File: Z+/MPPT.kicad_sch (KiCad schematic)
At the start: 15 parts, among them U8 LTC3130

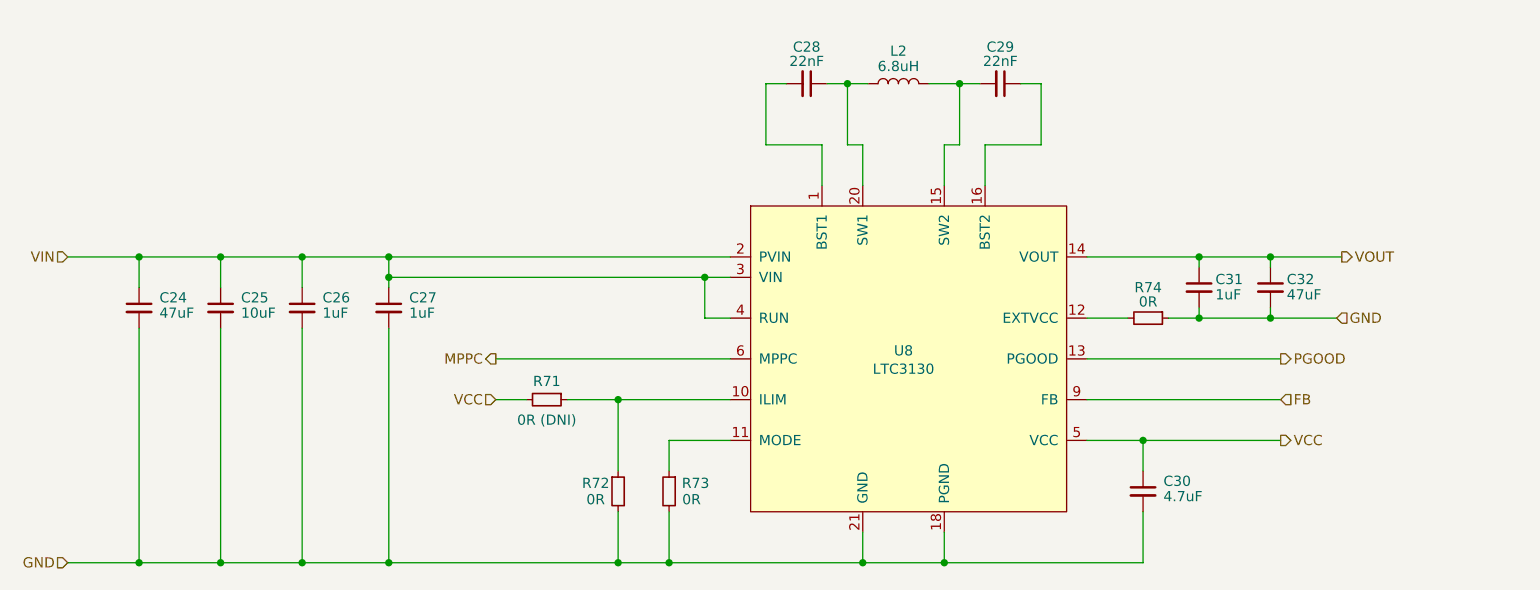
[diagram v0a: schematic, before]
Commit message: Added DRV8235, Quad Light Sensor, and refactored schematics
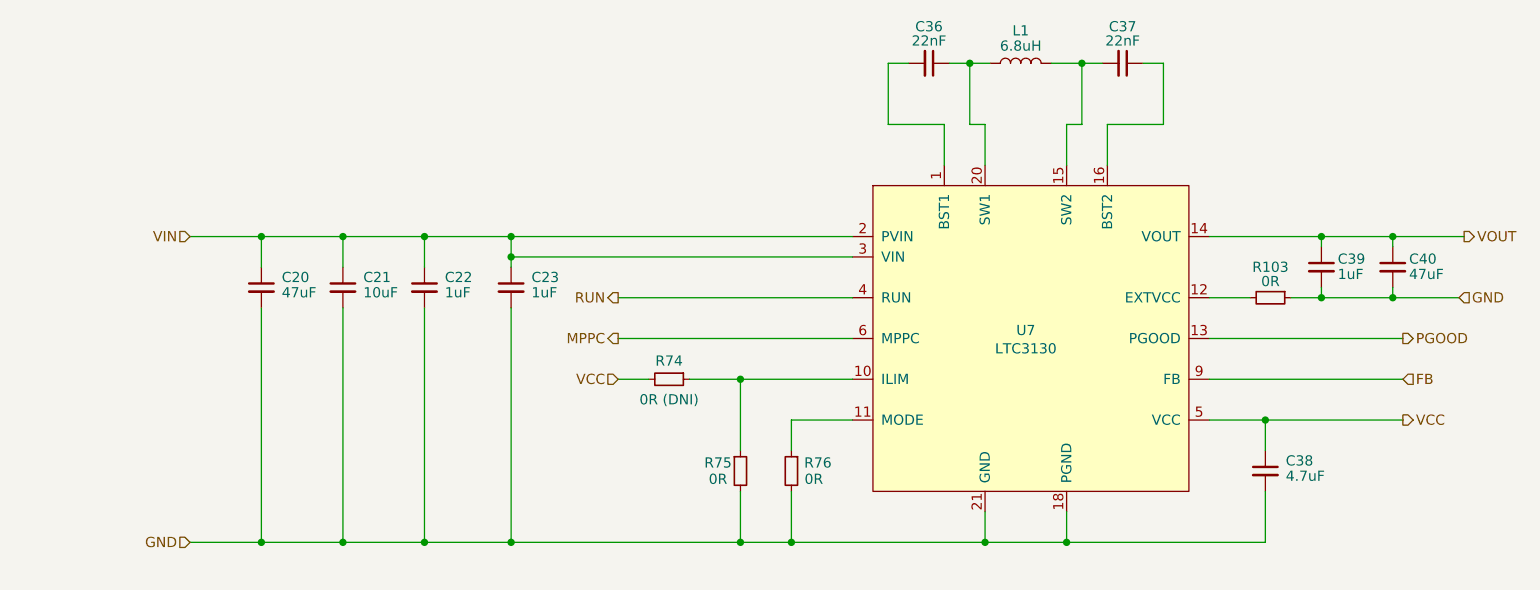
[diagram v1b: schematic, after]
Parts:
- removed C24, C32: 47uF, Capacitor_SMD:C_1210_3225Metric, symbol Device:C_Small
- removed C25: 10uF, Capacitor_SMD:C_1210_3225Metric, symbol Device:C_Small
- removed C26, C27, C31: 1uF, Capacitor_SMD:C_0805_2012Metric, symbol Device:C_Small
- removed C28, C29: 22nF, Capacitor_SMD:C_0603_1608Metric, symbol Device:C_Small
- removed C30: 4.7uF, Capacitor_SMD:C_0603_1608Metric, symbol Device:C_Small
- removed L2: 6.8uH, Inductor_SMD:L_Coilcraft_LPS4018, symbol Device:L
- removed R71: 0R (DNI), Resistor_SMD:R_0603_1608Metric, symbol Device:R_Small
- removed R72, R73: 0R, Resistor_SMD:R_0603_1608Metric, symbol Device:R_Small
- removed U8: LTC3130, Package_DFN_QFN:QFN-20-1EP_3x4mm_P0.5mm_EP1.65x2.65mm, symbol SolarPanels:LTC3130
- added C20, C40: 47uF, Capacitor_SMD:C_1210_3225Metric, symbol Device:C_Small
- added C21: 10uF, Capacitor_SMD:C_1210_3225Metric, symbol Device:C_Small
- added C22, C23, C39: 1uF, Capacitor_SMD:C_0805_2012Metric, symbol Device:C_Small
- added C36, C37: 22nF, Capacitor_SMD:C_0603_1608Metric, symbol Device:C_Small
- added C38: 4.7uF, Capacitor_SMD:C_0603_1608Metric, symbol Device:C_Small
- added L1: 6.8uH, Argus-Passives:L_Coilcraft_LPS4018, symbol Device:L
- added R103, R75, R76: 0R, Resistor_SMD:R_0603_1608Metric, symbol Device:R_Small
- added U7: LTC3130, Package_DFN_QFN:QFN-20-1EP_3x4mm_P0.5mm_EP1.65x2.65mm, symbol Argus-IC:LTC3130
- R74: value 0R -> 0R (DNI)
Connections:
- net FB: now also U7.9 (FB)
- net GND: now also C20.2, C21.2, C22.2, C23.2, C38.2, C39.2, C40.2, R103.1, R75.2, R76.2, U7.17 (GND), U7.18 (PGND), U7.19 (PGND), U7.21 (GND), U7.7 (GND), U7.8 (GND); no longer R74.1
- net MPPC: now also U7.6 (MPPC)
- net PGOOD: now also U7.13 (PGOOD)
- net VCC: now also R74.2, C38.1, U7.5 (VCC)
- net VIN: now also C20.1, C21.1, C22.1, C23.1, U7.2 (PVIN), U7.3 (VIN)
- net VOUT: now also C39.1, C40.1, U7.14 (VOUT)
- new net: C36.1, L1.1, U7.20 (SW1)
- new net: C36.2, U7.1 (BST1)
- new net: R74.1, R75.1, U7.10 (ILIM)
- new net: R76.1, U7.11 (MODE)
- new net: R103.2, U7.12 (EXTVCC)
- new net: C37.2, L1.2, U7.15 (SW2)
- new net: C37.1, U7.16 (BST2)
- new net RUN: U7.4 (RUN)

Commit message: Z+ updates WIP
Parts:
- renumbered C20 to C18, C21 to C19, C22 to C20, C23 to C21, C36 to C22, C37 to C23, C38 to C24, C39 to C25, C40 to C26, R74 to R58, R75 to R59, R76 to R60, R103 to R61, U7 to U9
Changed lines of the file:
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@@
 		(on_board yes)
 		(dnp no)
-		(property "Reference" "C36"
+		(property "Reference" "C22"
 			(at 156.845 61.468 90)
 			(effects
@@
 			(project "Z+"
 				(path "/977a45af-b6d4-4b54-8e70-e74e2c44e8e7/3495d2a7-7425-4e27-a34a-beb5018fad2a/da1acfbe-9fa7-42e1-87e1-6085a640b36c"
-					(reference "C36")
+					(reference "C22")
 					(unit 1)
 				)
@@
 		(on_board yes)
 		(dnp no)
-		(property "Reference" "R75"
+		(property "Reference" "R59"
 			(at 130.556 115.824 0)
 			(effects
@@
 			(project "Z+"
 				(path "/977a45af-b6d4-4b54-8e70-e74e2c44e8e7/3495d2a7-7425-4e27-a34a-beb5018fad2a/da1acfbe-9fa7-42e1-87e1-6085a640b36c"
-					(reference "R75")
+					(reference "R59")
 					(unit 1)
 				)
@@
 		(on_board yes)
 		(dnp no)
-		(property "Reference" "R76"
+		(property "Reference" "R60"
 			(at 143.002 115.824 0)
 			(effects
@@
 			(project "Z+"
 				(path "/977a45af-b6d4-4b54-8e70-e74e2c44e8e7/3495d2a7-7425-4e27-a34a-beb5018fad2a/da1acfbe-9fa7-42e1-87e1-6085a640b36c"
-					(reference "R76")
+					(reference "R60")
 					(unit 1)
 				)
@@
 		(on_board yes)
 		(dnp no)
-		(property "Reference" "C40"
+		(property "Reference" "C26"
 			(at 216.662 90.424 0)
 			(effects
@@
 			(project "Z+"
 				(path "/977a45af-b6d4-4b54-8e70-e74e2c44e8e7/3495d2a7-7425-4e27-a34a-beb5018fad2a/da1acfbe-9fa7-42e1-87e1-6085a640b36c"
-					(reference "C40")
+					(reference "C26")
 					(unit 1)
 				)
@@
 		(on_board yes)
 		(dnp no)
-		(property "Reference" "U7"
+		(property "Reference" "U9"
 			(at 168.91 99.314 0)
 			(effects
@@
 			(project "Z+"
 				(path "/977a45af-b6d4-4b54-8e70-e74e2c44e8e7/3495d2a7-7425-4e27-a34a-beb5018fad2a/da1acfbe-9fa7-42e1-87e1-6085a640b36c"
-					(reference "U7")
+					(reference "U9")
 					(unit 1)
 				)
@@
 		(on_board yes)
 		(dnp no)
-		(property "Reference" "C23"
+		(property "Reference" "C21"
 			(at 107.315 92.71 0)
 			(effects
@@
 			(project "Z+"
 				(path "/977a45af-b6d4-4b54-8e70-e74e2c44e8e7/3495d2a7-7425-4e27-a34a-beb5018fad2a/da1acfbe-9fa7-42e1-87e1-6085a640b36c"
-					(reference "C23")
+					(reference "C21")
 					(unit 1)
 				)
@@
 		(on_board yes)
 		(dnp no)
-		(property "Reference" "C22"
+		(property "Reference" "C20"
 			(at 96.52 92.71 0)
 			(effects
@@
 			(project "Z+"
 				(path "/977a45af-b6d4-4b54-8e70-e74e2c44e8e7/3495d2a7-7425-4e27-a34a-beb5018fad2a/da1acfbe-9fa7-42e1-87e1-6085a640b36c"
-					(reference "C22")
+					(reference "C20")
 					(unit 1)
 				)
@@
 		(on_board yes)
 		(dnp no)
-		(property "Reference" "R103"
+		(property "Reference" "R61"
 			(at 199.39 91.44 90)
 			(effects
@@
 			(project "Z+"
 				(path "/977a45af-b6d4-4b54-8e70-e74e2c44e8e7/3495d2a7-7425-4e27-a34a-beb5018fad2a/da1acfbe-9fa7-42e1-87e1-6085a640b36c"
-					(reference "R103")
+					(reference "R61")
 					(unit 1)
 				)
@@
 		(on_board yes)
 		(dnp no)
-		(property "Reference" "C20"
+		(property "Reference" "C18"
 			(at 76.2 92.71 0)
 			(effects
@@
 			(project "Z+"
 				(path "/977a45af-b6d4-4b54-8e70-e74e2c44e8e7/3495d2a7-7425-4e27-a34a-beb5018fad2a/da1acfbe-9fa7-42e1-87e1-6085a640b36c"
-					(reference "C20")
+					(reference "C18")
 					(unit 1)
 				)
@@
 		(on_board yes)
 		(dnp no)
-		(property "Reference" "R74"
+		(property "Reference" "R58"
 			(at 124.46 103.124 90)
 			(effects
@@
 			(project "Z+"
 				(path "/977a45af-b6d4-4b54-8e70-e74e2c44e8e7/3495d2a7-7425-4e27-a34a-beb5018fad2a/da1acfbe-9fa7-42e1-87e1-6085a640b36c"
-					(reference "R74")
+					(reference "R58")
 					(unit 1)
 				)
@@
 		(on_board yes)
 		(dnp no)
-		(property "Reference" "C38"
+		(property "Reference" "C24"
 			(at 201.295 115.57 0)
 			(effects
@@
 			(project "Z+"
 				(path "/977a45af-b6d4-4b54-8e70-e74e2c44e8e7/3495d2a7-7425-4e27-a34a-beb5018fad2a/da1acfbe-9fa7-42e1-87e1-6085a640b36c"
-					(reference "C38")
+					(reference "C24")
 					(unit 1)
 				)
@@
 		(on_board yes)
 		(dnp no)
-		(property "Reference" "C39"
+		(property "Reference" "C25"
 			(at 207.772 90.424 0)
 			(effects
@@
 			(project "Z+"
 				(path "/977a45af-b6d4-4b54-8e70-e74e2c44e8e7/3495d2a7-7425-4e27-a34a-beb5018fad2a/da1acfbe-9fa7-42e1-87e1-6085a640b36c"
-					(reference "C39")
+					(reference "C25")
 					(unit 1)
 				)
@@
 		(on_board yes)
 		(dnp no)
-		(property "Reference" "C37"
+		(property "Reference" "C23"
 			(at 180.975 61.468 90)
 			(effects
@@
 			(project "Z+"
 				(path "/977a45af-b6d4-4b54-8e70-e74e2c44e8e7/3495d2a7-7425-4e27-a34a-beb5018fad2a/da1acfbe-9fa7-42e1-87e1-6085a640b36c"
-					(reference "C37")
+					(reference "C23")
 					(unit 1)
 				)
@@
 		(on_board yes)
 		(dnp no)
-		(property "Reference" "C21"
+		(property "Reference" "C19"
 			(at 86.36 92.71 0)
 			(effects
@@
 			(project "Z+"
 				(path "/977a45af-b6d4-4b54-8e70-e74e2c44e8e7/3495d2a7-7425-4e27-a34a-beb5018fad2a/da1acfbe-9fa7-42e1-87e1-6085a640b36c"
-					(reference "C21")
-					(unit 1)
-				)
+					(reference "C19")
+					(unit 1)
+				)
